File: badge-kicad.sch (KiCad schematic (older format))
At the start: 109 parts, among them J2 JTAG, P2 CONN_02X20, P3 FTDI BACKUP, P4 USB_MICRO_RIGHT, P5 LED OUT (DNP), SW1 RESET, SW2 POWERON, SW3 TM1000, SW4 UP, SW5 DN, SW6 LEFT, SW7 RIGHT, SW8 ENTER, U1 WS2812B, U10 WS2812B, U11 WS2812B, U12 WS2812B, U13 MKW01Z128, U14 FT232RL SSOP, U15 MF-REG-SOT235-3.3V-300mA, U16 MCP73831T-2ACI/OT, U2 WS2812B, U3 WS2812B, U4 WS2812B, U5 WS2812B, U6 WS2812B, U7 WS2812B, U8 WS2812B, U9 WS2812B, Y1 EXS00A-CS02368

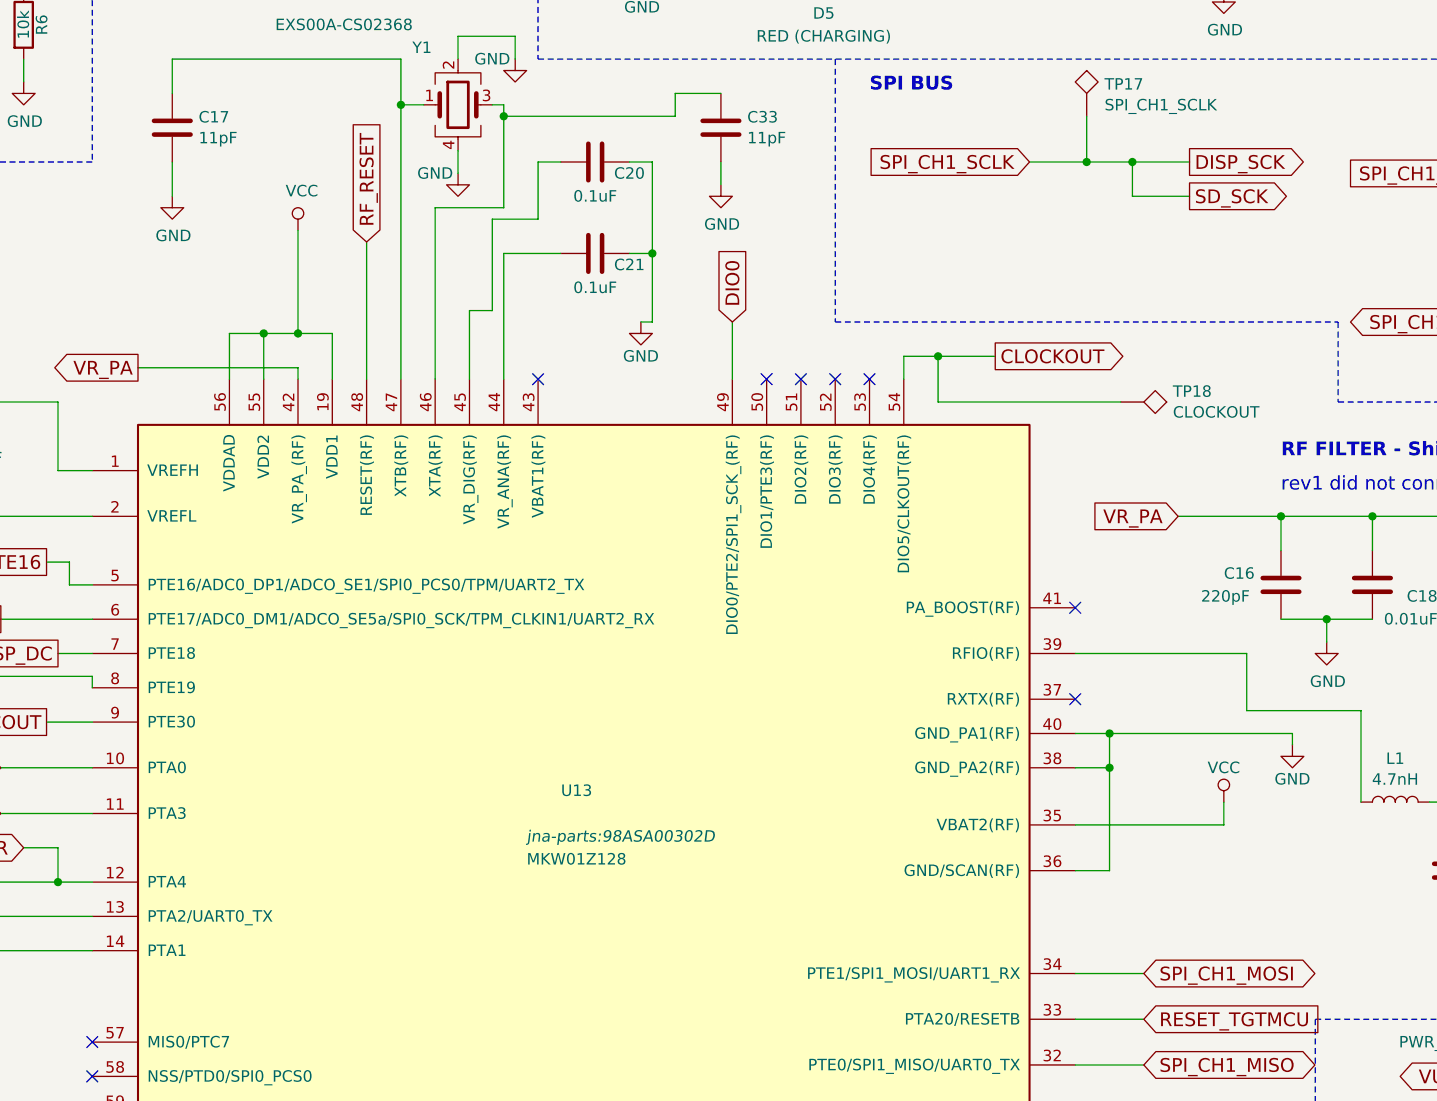
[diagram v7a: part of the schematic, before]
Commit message: Revision 2 final layout.
Add connection for missing VBAT connector, add some decoupling caps on KW01
Output drill files again.
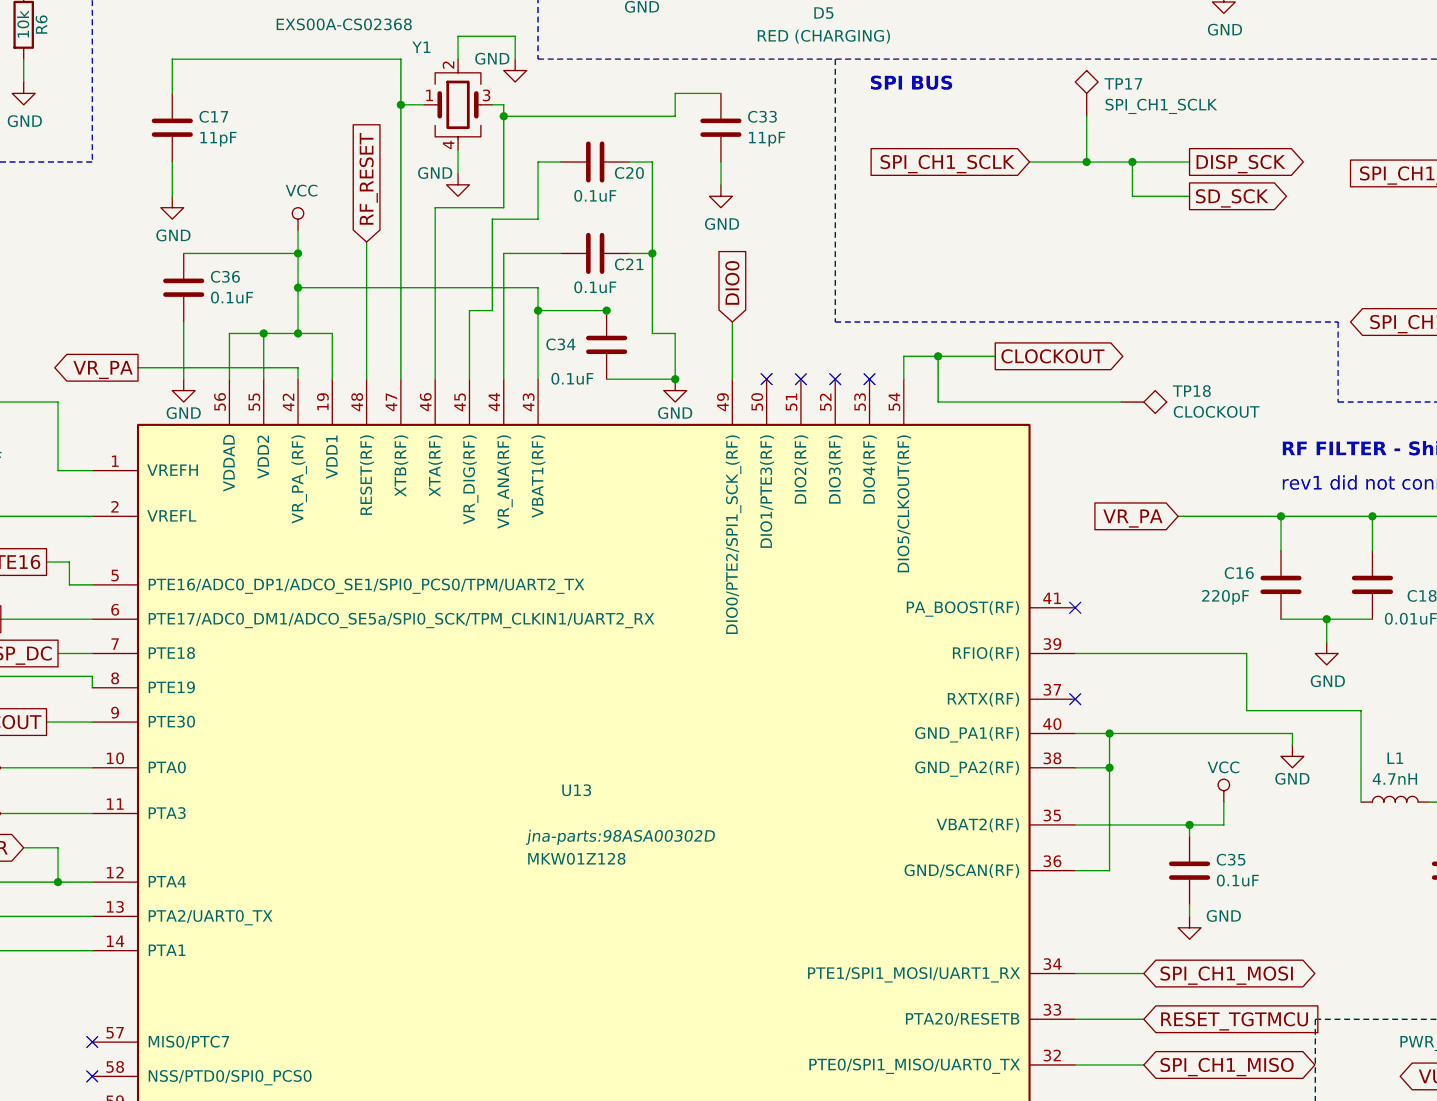
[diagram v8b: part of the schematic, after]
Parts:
- added C34, C35, C36: 0.1uF, Capacitors_SMD:C_0805_HandSoldering, symbol C
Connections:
- net GND: now also C34.1, C35.2, C36.2
- net VCC: now also U13.43 (VBAT1(RF)), C34.2, C35.1, C36.1
- no-connect marks 63 -> 62
